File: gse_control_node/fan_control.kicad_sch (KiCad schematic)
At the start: 5 parts, among them J2 Conn_01x04, Q6 BSS138

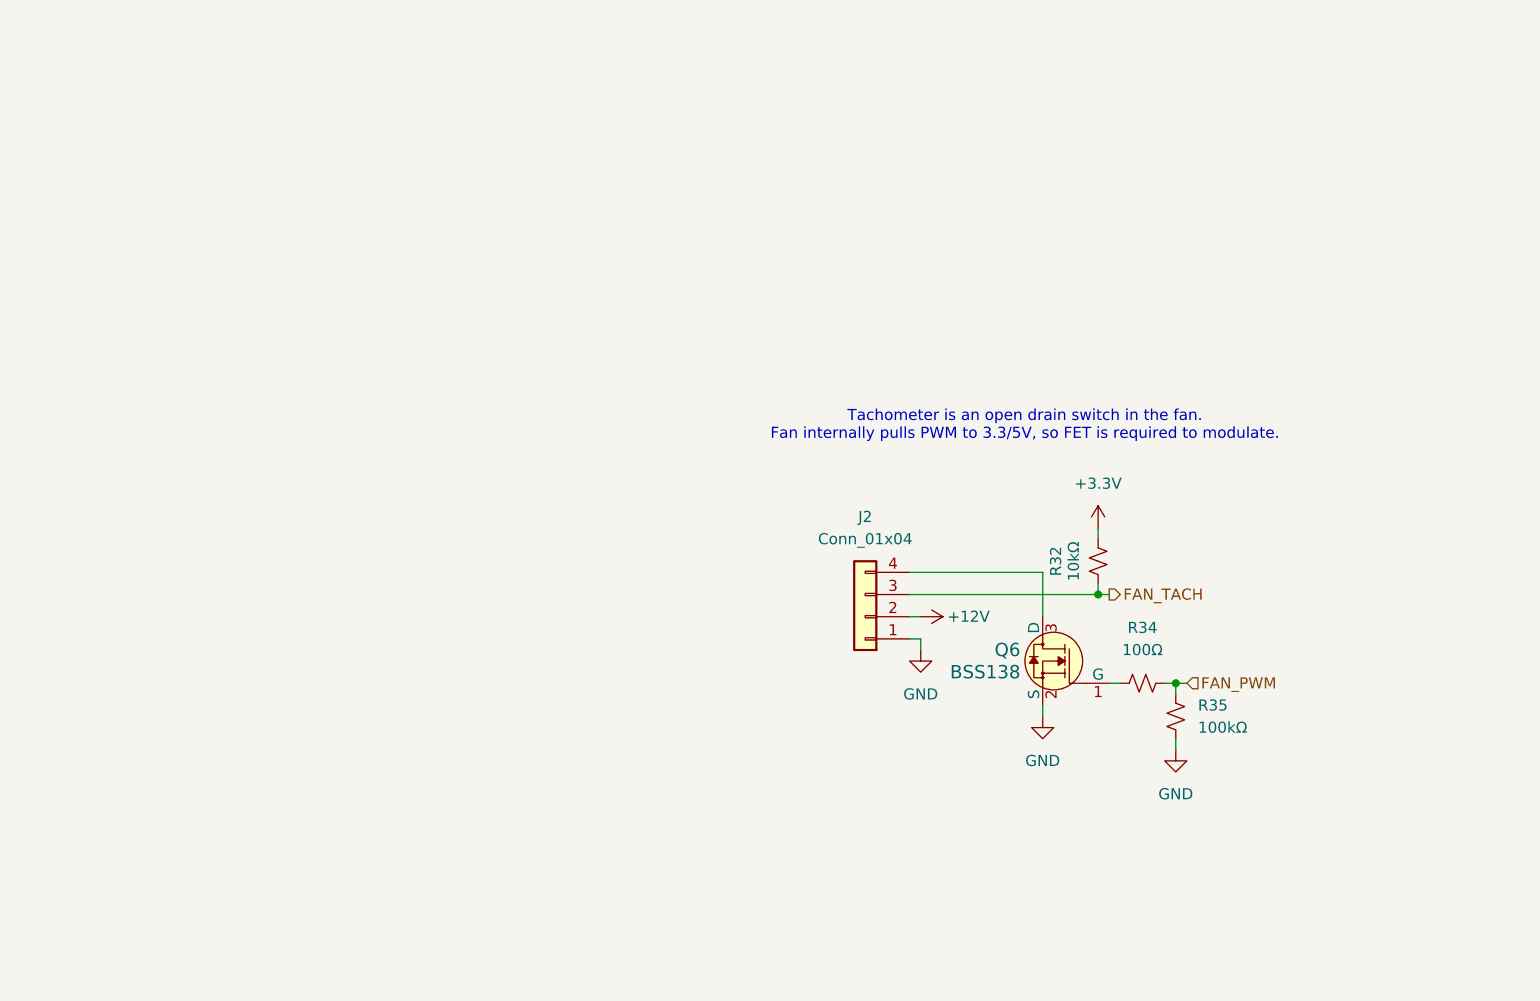
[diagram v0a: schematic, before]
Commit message: finish control board routing
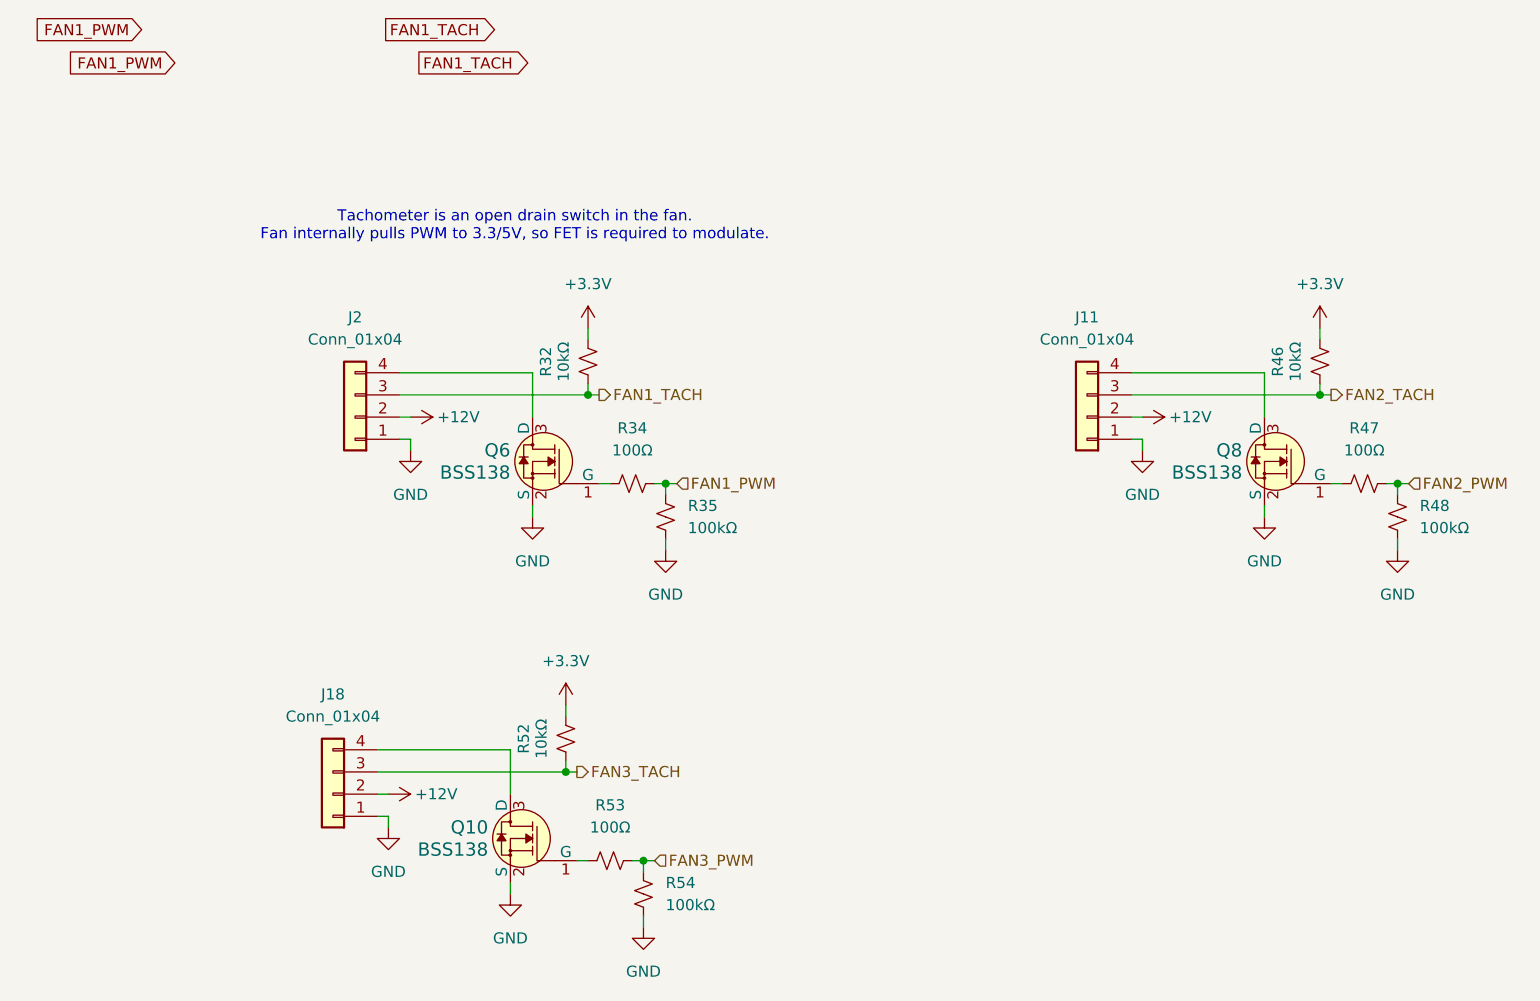
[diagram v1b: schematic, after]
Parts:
- added J11, J18: Conn_01x04, Connector_Molex:Molex_KK-254_AE-6410-04A_1x04_P2.54mm_Vertical, symbol Connector_Generic:Conn_01x04
- added Q10, Q8: BSS138, Package_TO_SOT_SMD:SOT-23-3, symbol dk_Transistors-FETs-MOSFETs-Single:BSS138
- added R46, R52: 10kΩ, Resistor_SMD:R_0603_1608Metric, symbol Device:R_Small_US
- added R47, R53: 100Ω, Resistor_SMD:R_0603_1608Metric, symbol Device:R_Small_US
- added R48, R54: 100kΩ, Resistor_SMD:R_0603_1608Metric, symbol Device:R_Small_US
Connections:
- net +12V: now also J11.2 (Pin_2), J18.2 (Pin_2)
- net +3.3V: now also R46.2, R52.2
- net GND: now also J11.1 (Pin_1), J18.1 (Pin_1), Q10.2 (S), Q8.2 (S), R48.2, R54.2
- net FAN_PWM renamed FAN1_PWM
- net FAN_TACH renamed FAN1_TACH
- new net: J18.4 (Pin_4), Q10.3 (D)
- new net: J11.4 (Pin_4), Q8.3 (D)
- new net: Q8.1 (G), R47.1
- new net: Q10.1 (G), R53.1
- new net FAN2_PWM: R47.2, R48.1
- new net FAN2_TACH: J11.3 (Pin_3), R46.1
- new net FAN3_PWM: R53.2, R54.1
- new net FAN3_TACH: J18.3 (Pin_3), R52.1
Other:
- moved on the sheet: J2, Q6, R32, R34, R35

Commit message: updates for manufacturing
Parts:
- J11, J18, J2, Q10, Q6, Q8: now in the parts list
- R32, R46, R52: value 10kΩ -> 10k
- R34, R47, R53: value 100Ω -> 100
- R35, R48, R54: value 100kΩ -> 100k
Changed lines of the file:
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@@
 			)
 		)
-		(property "Value" "100kΩ"
+		(property "Value" "100k"
 			(at 74.93 58.4199 0)
 			(show_name no)
@@
 		(body_style 1)
 		(exclude_from_sim no)
-		(in_bom no)
-		(on_board yes)
-		(in_pos_files no)
+		(in_bom yes)
+		(on_board yes)
+		(in_pos_files yes)
 		(dnp no)
 		(fields_autoplaced yes)
@@
 			)
 		)
-		(property "Value" "100kΩ"
+		(property "Value" "100k"
 			(at 72.39 101.5999 0)
 			(show_name no)
@@
 		(body_style 1)
 		(exclude_from_sim no)
-		(in_bom no)
-		(on_board yes)
-		(in_pos_files no)
+		(in_bom yes)
+		(on_board yes)
+		(in_pos_files yes)
 		(dnp no)
 		(property "Reference" "Q6"
@@
 			)
 		)
-		(property "Value" "10kΩ"
+		(property "Value" "10k"
 			(at 58.166 82.55 90)
 			(show_name no)
@@
 		(body_style 1)
 		(exclude_from_sim no)
-		(in_bom no)
-		(on_board yes)
-		(in_pos_files no)
+		(in_bom yes)
+		(on_board yes)
+		(in_pos_files yes)
 		(dnp no)
 		(fields_autoplaced yes)
@@
 			)
 		)
-		(property "Value" "100Ω"
+		(property "Value" "100"
 			(at 152.4 49.53 90)
 			(show_name no)
@@
 		(body_style 1)
 		(exclude_from_sim no)
-		(in_bom no)
-		(on_board yes)
-		(in_pos_files no)
+		(in_bom yes)
+		(on_board yes)
+		(in_pos_files yes)
 		(dnp no)
 		(property "Reference" "Q8"
@@
 			)
 		)
-		(property "Value" "100kΩ"
+		(property "Value" "100k"
 			(at 158.75 58.4199 0)
 			(show_name no)
@@
 			)
 		)
-		(property "Value" "10kΩ"
+		(property "Value" "10k"
 			(at 60.706 39.37 90)
 			(show_name no)
@@
 			)
 		)
-		(property "Value" "100Ω"
+		(property "Value" "100"
 			(at 68.58 49.53 90)
 			(show_name no)
@@
 		(body_style 1)
 		(exclude_from_sim no)
-		(in_bom no)
-		(on_board yes)
-		(in_pos_files no)
+		(in_bom yes)
+		(on_board yes)
+		(in_pos_files yes)
 		(dnp no)
 		(property "Reference" "Q10"
@@
 		(body_style 1)
 		(exclude_from_sim no)
-		(in_bom no)
-		(on_board yes)
-		(in_pos_files no)
+		(in_bom yes)
+		(on_board yes)
+		(in_pos_files yes)
 		(dnp no)
 		(fields_autoplaced yes)
@@
 			)
 		)
-		(property "Value" "100Ω"
+		(property "Value" "100"
 			(at 66.04 92.71 90)
 			(show_name no)
@@
 			)
 		)
-		(property "Value" "10kΩ"
+		(property "Value" "10k"
 			(at 144.526 39.37 90)
 			(show_name no)
